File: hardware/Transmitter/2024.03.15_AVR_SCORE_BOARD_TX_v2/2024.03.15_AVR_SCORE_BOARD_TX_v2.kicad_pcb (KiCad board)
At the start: 2 copper layers, 44 parts, among them J1 Conn_01x10, J2 Conn_01x10, J3 Conn_01x05, Q1 BC817, SW1 SW_D1S+, SW10 D2S-, SW11 D2P+, SW12 D2P-, SW2 D1S-, SW3 SW_D1P+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

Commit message: Added LP2980 voltage regulator for NRF24L01
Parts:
- added C5: 100nF, Capacitor_SMD:C_0805_2012Metric_Pad1.15x1.40mm_HandSolder, B.Cu at (132.0, 39.6)
- added U5: LP2980IM5-30_NOPB, Package_TO_SOT_SMD:SOT-23-5, B.Cu at (132.8, 47.4)
- BT1: value Battery_Cell -> 18650
- C4: value 100nF -> 2,2uF
- R1: value r -> 250k
- R2: value r -> 47k
- U4: value NRF24l04 -> NRF24l01
- moved U4 0.06 mm to (127.3, 53.0)
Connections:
- C4 pad 1: VCC -> Net-(C4-Pad1)
- U4 pad 2: VCC -> Net-(C4-Pad1)
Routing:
- net GND: track 65.1 -> 78.7 mm, vias 6 -> 8
- net Net-(C4-Pad1): track 0.00 -> 12.6 mm
- net COL1: track 52.2 -> 59.4 mm
- net LED_LOW_BAT: track 40.4 -> 45.8 mm

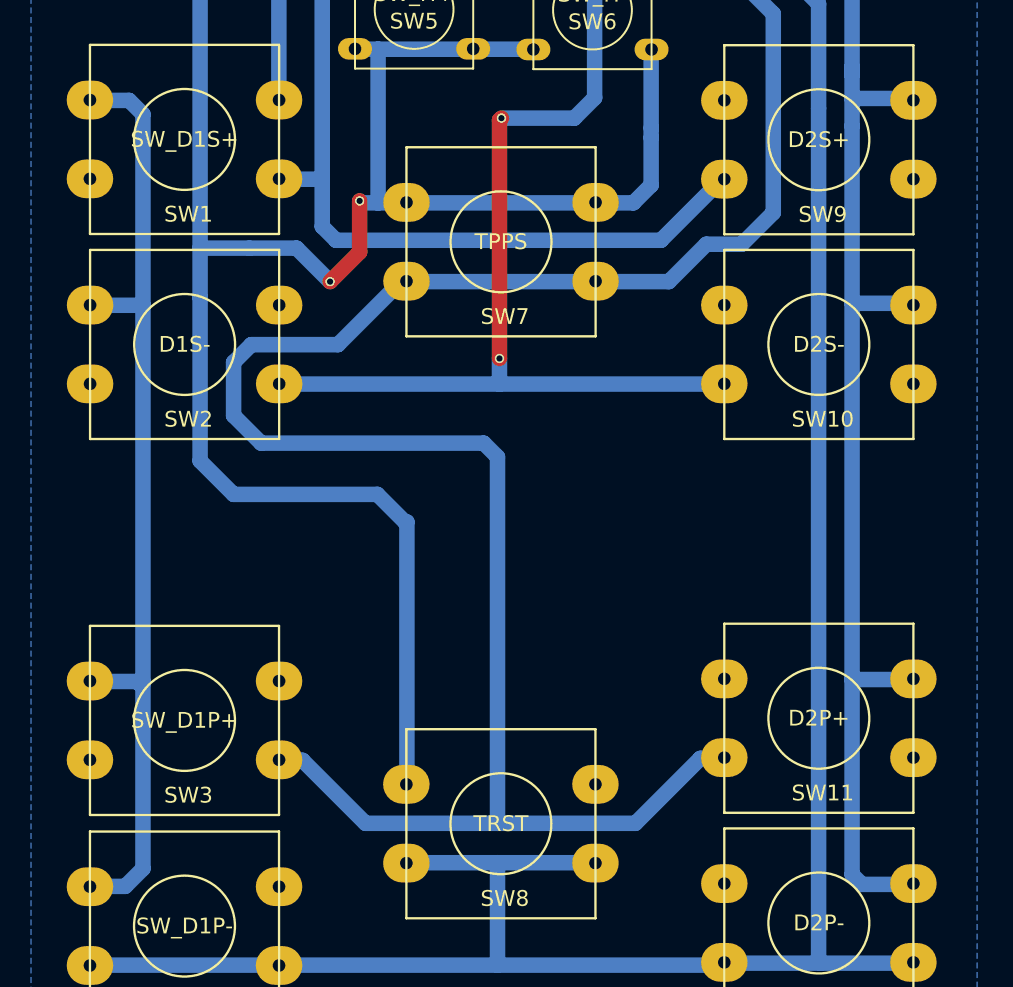
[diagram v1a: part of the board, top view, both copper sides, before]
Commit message: RCV Hardware updated - Voltage regulation
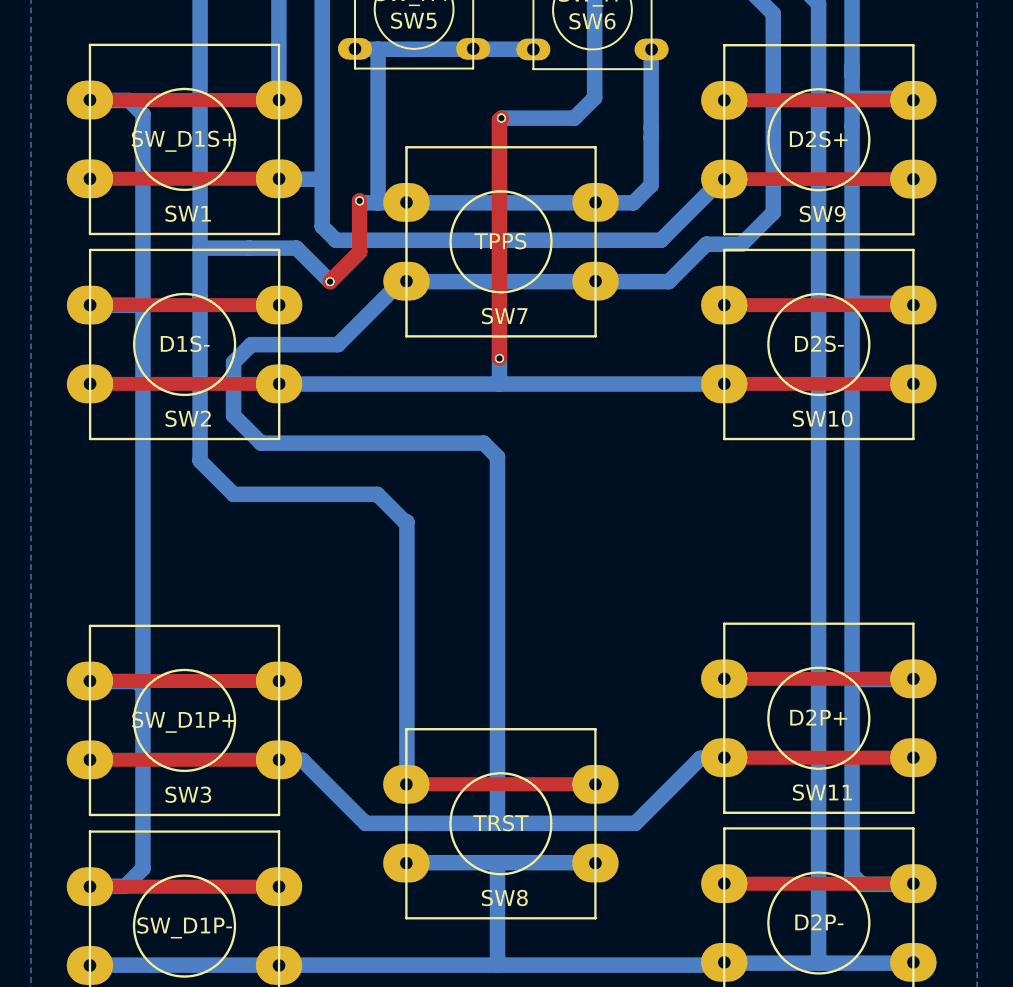
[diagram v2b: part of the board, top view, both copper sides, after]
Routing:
- net K_COL1: track 113.1 -> 161.9 mm
- net K_COL3: track 97.5 -> 146.3 mm
- net K_ROW2: track 79.6 -> 104.0 mm
- net K_ROW3: track 144.8 -> 169.2 mm
- net K_ROW1: track 69.7 -> 94.1 mm
- net K_COL2: track 153.3 -> 165.5 mm

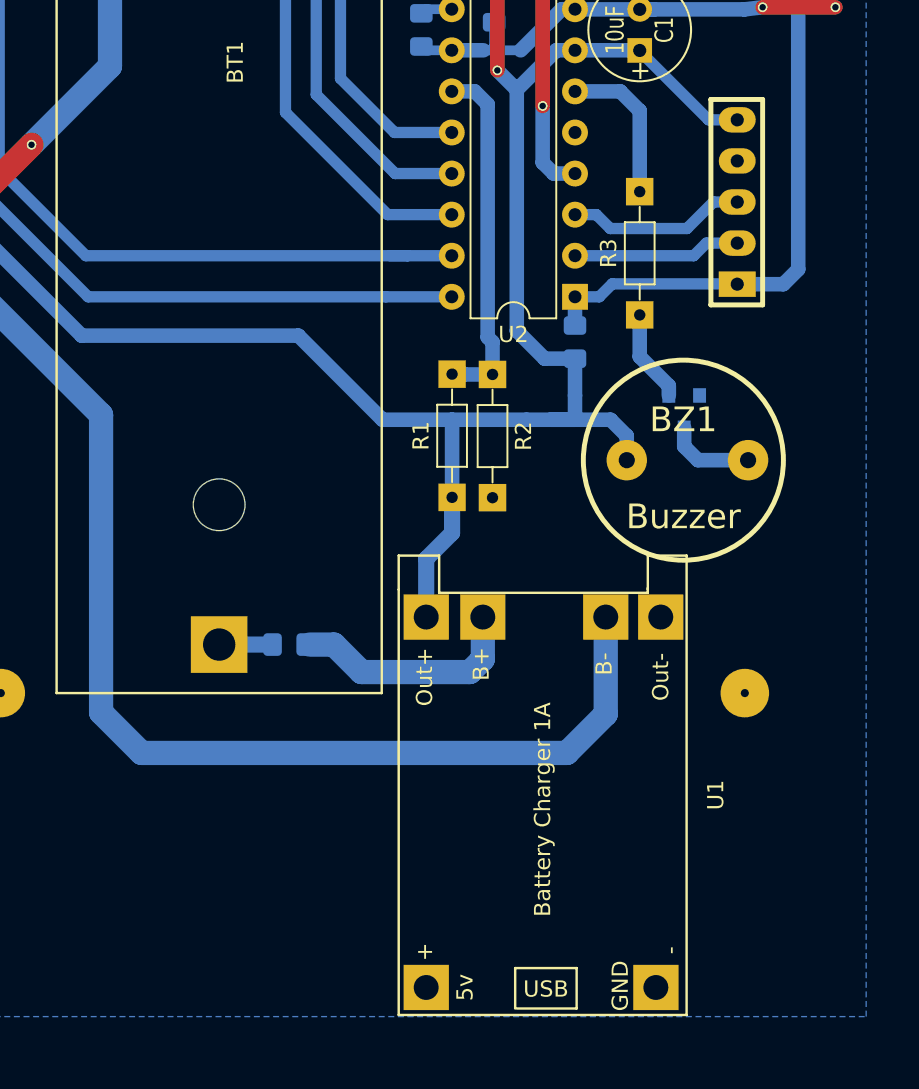
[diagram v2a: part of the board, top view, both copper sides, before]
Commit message: Added USB_B for charging and moved old schematic
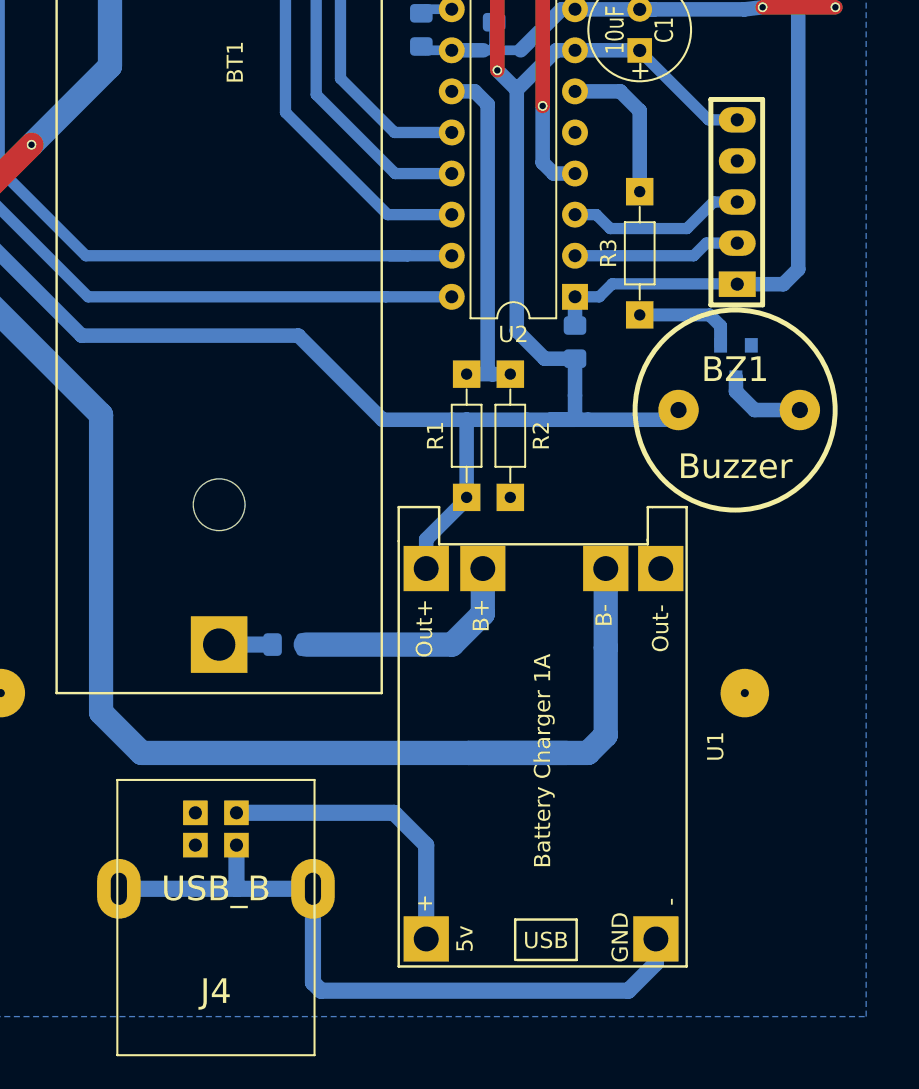
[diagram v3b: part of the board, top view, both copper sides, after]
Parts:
- added J4: USB_B, Moje:USB_B, F.Cu at (108.8, 138.6)
- moved BZ1 4.46 mm to (140.9, 109.0)
- moved Q1 4.46 mm to (140.9, 106.0)
- moved U1 3.00 mm to (120.1, 143.4)
- moved R2 1.10 mm to (127.0, 106.8)
- moved R1 0.90 mm to (124.3, 114.4)
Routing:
- net Net-(J4-Pad4): track 0.00 -> 44.1 mm
- net Net-(J4-Pad1): track 0.00 -> 18.4 mm
- net Net-(BT1-Pad2): track 128.4 -> 138.0 mm
- net VCC: track 236.3 -> 235.2 mm
- net Net-(Q1-Pad1): track 5.73 -> 6.48 mm
